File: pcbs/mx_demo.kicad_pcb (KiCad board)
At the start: 2 copper layers, 230 x 95 mm, 88 parts

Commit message: Add rectangular JST PH jumper variant and rendered board comparison
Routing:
- net c1: track 0.00 -> 105.8 mm, vias 0 -> 10
- net c1_r5: track 0.00 -> 23.1 mm, vias 0 -> 1
- net c1_r4: track 0.00 -> 23.1 mm, vias 0 -> 1
- net c1_r3: track 0.00 -> 23.1 mm, vias 0 -> 1
- net c1_r2: track 0.00 -> 23.1 mm, vias 0 -> 1
- net c1_r1: track 0.00 -> 23.1 mm, vias 0 -> 1
- net mirror_c1_r5: track 0.00 -> 23.1 mm, vias 0 -> 1
- net mirror_c1_r4: track 0.00 -> 23.1 mm, vias 0 -> 1
- net mirror_c1_r3: track 0.00 -> 23.1 mm, vias 0 -> 1
- net mirror_c1_r2: track 0.00 -> 23.1 mm, vias 0 -> 1
- net mirror_c1_r1: track 0.00 -> 23.1 mm, vias 0 -> 1
- net SDA: track 21.0 -> 0.00 mm
- net SCL: track 21.0 -> 0.00 mm
- net GND: track 36.0 -> 15.0 mm
- net CS: track 21.0 -> 0.00 mm
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
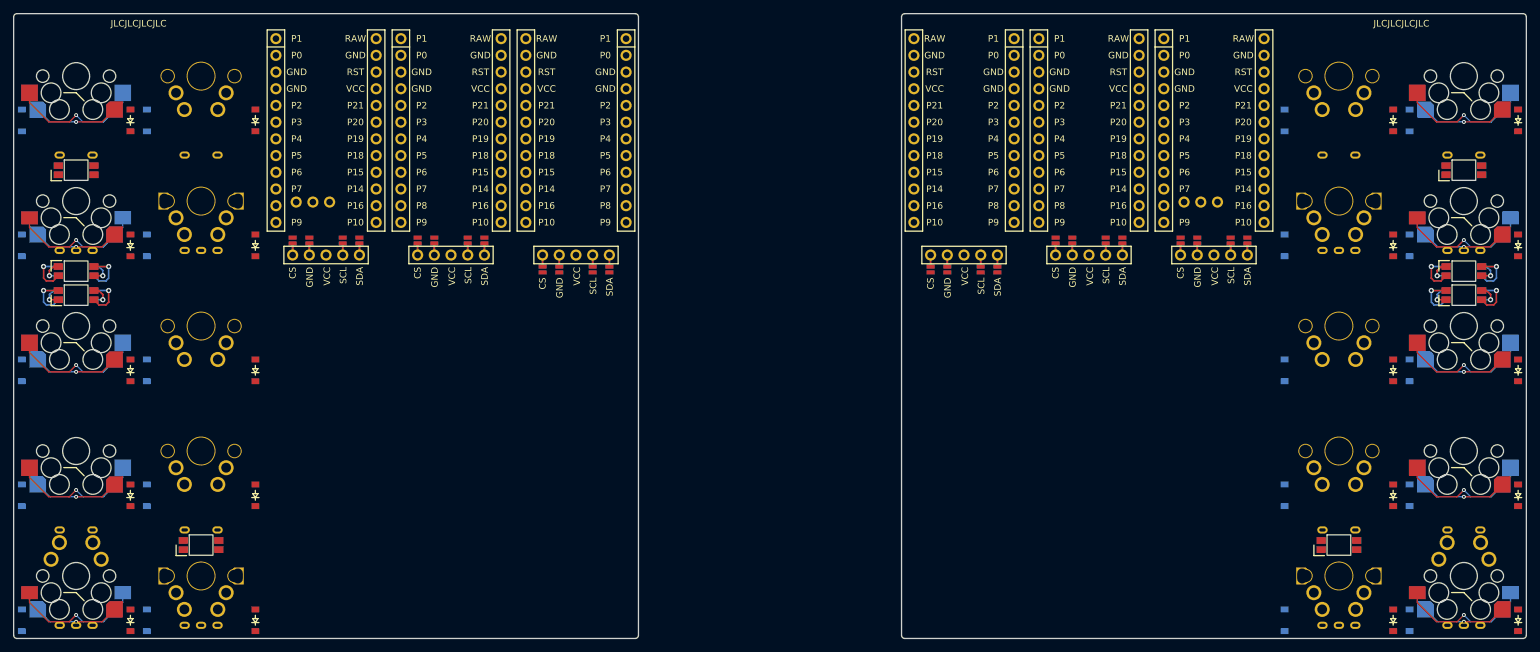
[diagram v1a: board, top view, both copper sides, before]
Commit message: Demonstrate pad-center traces with full-board and copper renders
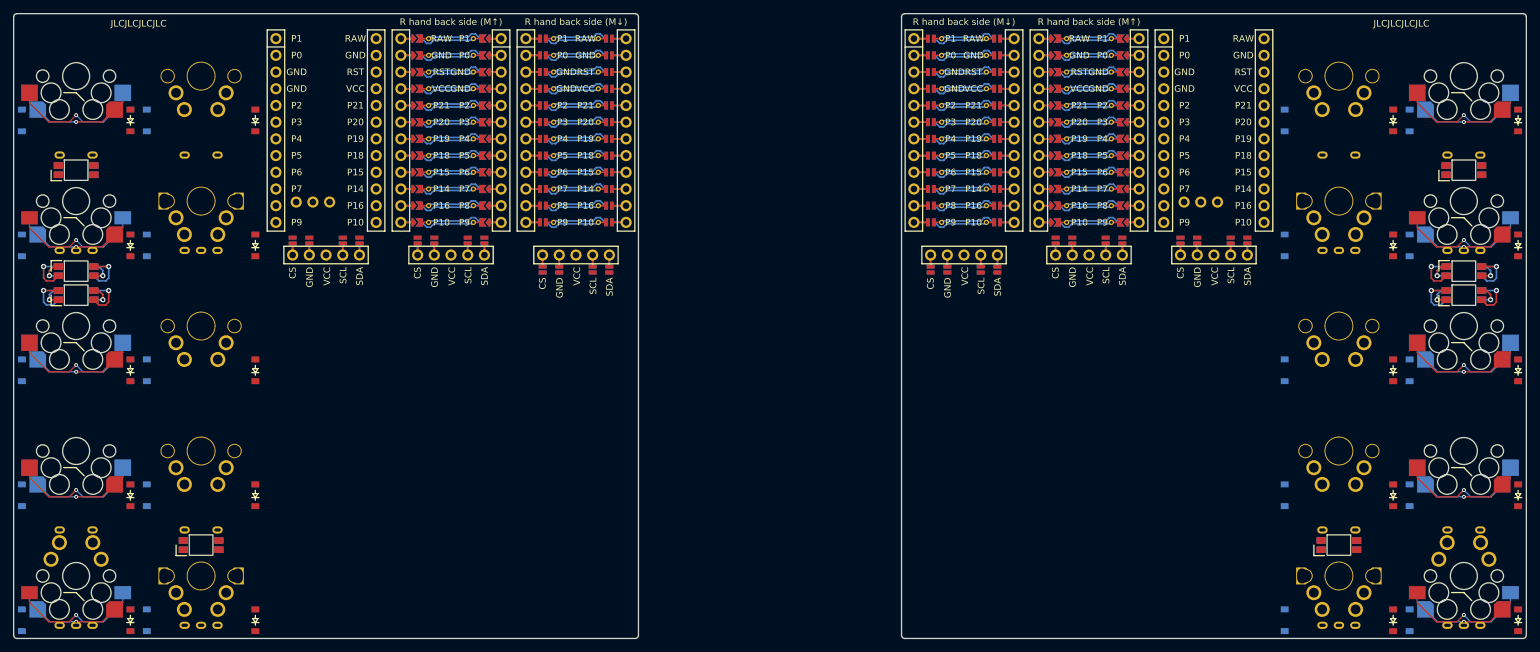
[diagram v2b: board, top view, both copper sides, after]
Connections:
- MCU1 pad 1: P1 -> MCU1_1
- MCU1 pad 10: P7 -> MCU1_10
- MCU1 pad 11: P8 -> MCU1_11
- MCU1 pad 12: P9 -> MCU1_12
- MCU1 pad 13: P10 -> MCU1_13
- MCU1 pad 14: P16 -> MCU1_14
- MCU1 pad 15: P14 -> MCU1_15
- MCU1 pad 16: P15 -> MCU1_16
- MCU1 pad 17: P18 -> MCU1_17
- MCU1 pad 18: P19 -> MCU1_18
- MCU1 pad 19: P20 -> MCU1_19
- MCU1 pad 2: P0 -> MCU1_2
- MCU1 pad 20: P21 -> MCU1_20
- MCU1 pad 21: VCC -> MCU1_21
- MCU1 pad 22: RST -> MCU1_22
- MCU1 pad 23: GND -> MCU1_23
- MCU1 pad 24: RAW -> MCU1_24
- MCU1 pad 3: GND -> MCU1_3
- MCU1 pad 4: GND -> MCU1_4
- MCU1 pad 5: P2 -> MCU1_5
- MCU1 pad 6: P3 -> MCU1_6
- MCU1 pad 7: P4 -> MCU1_7
- MCU1 pad 8: P5 -> MCU1_8
- MCU1 pad 9: P6 -> MCU1_9
- MCU2 pad 1: P1 -> MCU2_1
- MCU2 pad 10: P7 -> MCU2_10
- MCU2 pad 11: P8 -> MCU2_11
- MCU2 pad 12: P9 -> MCU2_12
- MCU2 pad 13: P10 -> MCU2_13
- MCU2 pad 14: P16 -> MCU2_14
- MCU2 pad 15: P14 -> MCU2_15
- MCU2 pad 16: P15 -> MCU2_16
- MCU2 pad 17: P18 -> MCU2_17
- MCU2 pad 18: P19 -> MCU2_18
- MCU2 pad 19: P20 -> MCU2_19
- MCU2 pad 2: P0 -> MCU2_2
- MCU2 pad 20: P21 -> MCU2_20
- MCU2 pad 21: VCC -> MCU2_21
- MCU2 pad 22: RST -> MCU2_22
- MCU2 pad 23: GND -> MCU2_23
- MCU2 pad 24: RAW -> MCU2_24
- MCU2 pad 3: GND -> MCU2_3
- MCU2 pad 4: GND -> MCU2_4
- MCU2 pad 5: P2 -> MCU2_5
- MCU2 pad 6: P3 -> MCU2_6
- MCU2 pad 7: P4 -> MCU2_7
- MCU2 pad 8: P5 -> MCU2_8
- MCU2 pad 9: P6 -> MCU2_9
- MCU3 pad 1: RAW -> MCU3_1
- MCU3 pad 10: P14 -> MCU3_10
- MCU3 pad 11: P16 -> MCU3_11
- MCU3 pad 12: P10 -> MCU3_12
- MCU3 pad 13: P9 -> MCU3_13
- MCU3 pad 14: P8 -> MCU3_14
- MCU3 pad 15: P7 -> MCU3_15
- MCU3 pad 16: P6 -> MCU3_16
- MCU3 pad 17: P5 -> MCU3_17
- MCU3 pad 18: P4 -> MCU3_18
- MCU3 pad 19: P3 -> MCU3_19
- MCU3 pad 2: GND -> MCU3_2
- MCU3 pad 20: P2 -> MCU3_20
- MCU3 pad 21: GND -> MCU3_21
- MCU3 pad 22: GND -> MCU3_22
- MCU3 pad 23: P0 -> MCU3_23
- MCU3 pad 24: P1 -> MCU3_24
- MCU3 pad 3: RST -> MCU3_3
- MCU3 pad 4: VCC -> MCU3_4
- MCU3 pad 5: P21 -> MCU3_5
- MCU3 pad 6: P20 -> MCU3_6
- MCU3 pad 7: P19 -> MCU3_7
- MCU3 pad 8: P18 -> MCU3_8
- MCU3 pad 9: P15 -> MCU3_9
- MCU4 pad 1: RAW -> MCU4_1
- MCU4 pad 10: P14 -> MCU4_10
- MCU4 pad 11: P16 -> MCU4_11
- MCU4 pad 12: P10 -> MCU4_12
- MCU4 pad 13: P9 -> MCU4_13
- MCU4 pad 14: P8 -> MCU4_14
- MCU4 pad 15: P7 -> MCU4_15
- MCU4 pad 16: P6 -> MCU4_16
- MCU4 pad 17: P5 -> MCU4_17
- MCU4 pad 18: P4 -> MCU4_18
- MCU4 pad 19: P3 -> MCU4_19
- MCU4 pad 2: GND -> MCU4_2
- MCU4 pad 20: P2 -> MCU4_20
- MCU4 pad 21: GND -> MCU4_21
- MCU4 pad 22: GND -> MCU4_22
- MCU4 pad 23: P0 -> MCU4_23
- MCU4 pad 24: P1 -> MCU4_24
- MCU4 pad 3: RST -> MCU4_3
- MCU4 pad 4: VCC -> MCU4_4
- MCU4 pad 5: P21 -> MCU4_5
- MCU4 pad 6: P20 -> MCU4_6
- MCU4 pad 7: P19 -> MCU4_7
- MCU4 pad 8: P18 -> MCU4_8
- MCU4 pad 9: P15 -> MCU4_9
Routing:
- net (no net): track 0.00 -> 1364.7 mm
- net c1: track 105.8 -> 204.4 mm
- net c1_r5: track 23.1 -> 13.2 mm
- net c1_r4: track 23.1 -> 13.2 mm
- net c1_r3: track 23.1 -> 13.2 mm
- net c1_r2: track 23.1 -> 13.2 mm
- net c1_r1: track 23.1 -> 13.2 mm
- net mirror_c1_r5: track 23.1 -> 13.2 mm
- net mirror_c1_r4: track 23.1 -> 13.2 mm
- net mirror_c1_r3: track 23.1 -> 13.2 mm
- net mirror_c1_r2: track 23.1 -> 13.2 mm
- net mirror_c1_r1: track 23.1 -> 13.2 mm
